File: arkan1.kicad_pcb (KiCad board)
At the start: 2 copper layers, 64.3 x 73 mm, 40 parts, among them J1 Conn_01x02, J2 USB_C_Receptacle_USB2.0_16P, J3 Conn_Coaxial, J4 Conn_Coaxial, Q1 NMOS (DSG), Q2 NMOS (CHG), Q3 PMOS, SW1 SW_Push, U1 DW01A, U2 SX1278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

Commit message: updated pcb
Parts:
- removed J3: Conn_Coaxial, Connector_Coaxial:SMA_Molex_73251-1153_EdgeMount_Horizontal
- C7: value 4.7 uF -> 1 uF
- C8: value 4.7 uF -> 1 uf
- D1, D2, D3: footprint LED_SMD:LED_0201_0603Metric -> LED_SMD:LED_0805_2012Metric
- R1, R10, R11, R13, R2, R3, R4, R5, R6, R7, R9: footprint Resistor_SMD:R_0201_0603Metric -> Resistor_SMD:R_0805_2012Metric_Pad1.20x1.40mm_HandSolder
- SW1: footprint Button_Switch_SMD:Nidec_Copal_CAS-120A -> Button_Switch_SMD:SW_SPST_PTS645Sx43SMTR92
- U2: value SX1278 -> Ai-Thinker-Ra-02; footprint Package_DFN_QFN:QFN-28-1EP_6x6mm_P0.65mm_EP4.8x4.8mm -> RF_Module:Ai-Thinker-Ra-01-LoRa
- U3: footprint Package_SO:SOIC-8-1EP_3.9x4.9mm_P1.27mm_EP2.41x3.3mm_ThermalVias -> Package_SO:SOIC-8-1EP_3.9x4.9mm_P1.27mm_EP2.41x3.81mm
- moved R4 6.60 mm to (211.6, 83.5)
- moved U2 6.08 mm to (183.7, 123.0), turned to 0 degrees
- moved C1 5.15 mm to (186.6, 87.7)
- moved L1 3.93 mm to (189.1, 110.0)
- moved R11 3.93 mm to (193.5, 110.0)
- moved C10 3.81 mm to (195.3, 92.2)
- moved R1 2.76 mm to (178.1, 81.6)
- moved SW1 2.76 mm to (179.5, 88.8)
- moved D3 1.67 mm to (189.7, 106.0)
- moved R3 1.12 mm to (192.2, 65.4)
- moved R7 1.12 mm to (192.2, 63.2)
- moved R2 1.07 mm to (198.4, 75.4)
- moved R6 1.01 mm to (211.8, 78.4)
- moved R5 0.87 mm to (211.8, 75.7)
- moved R13 0.83 mm to (178.6, 77.7)
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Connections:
- A1 pad 13: Net-(A1-GND-Pad13) -> GND
- A1 pad 18: Net-(A1-GND-Pad13) -> GND
- A1 pad 23: Net-(A1-GND-Pad13) -> GND
- A1 pad 24: Net-(A1-GPIO18) -> unconnected-(A1-GPIO18-Pad24)
- A1 pad 27: unconnected-(A1-GPIO21-Pad27) -> Net-(A1-GPIO21)
- A1 pad 3: Net-(A1-GND-Pad13) -> GND
- A1 pad 33: unconnected-(A1-AGND-Pad33) -> GND
- A1 pad 38: Net-(A1-GND-Pad13) -> GND
- A1 pad 8: Net-(A1-GND-Pad13) -> GND
- J2 pad B6: unconnected-(J2-D+-PadA6) -> unconnected-(J2-D+-PadB6)
- J2 pad B7: unconnected-(J2-D--PadA7) -> unconnected-(J2-D--PadB7)
- U2 pad 1: Net-(J3-In) -> GND
- U2 pad 12: unconnected-(U2-DIO4-Pad12) -> Net-(A1-GPIO19)
- U2 pad 13: unconnected-(U2-DIO5-Pad13) -> Net-(A1-GPIO22)
- U2 pad 14: Net-(A1-3V3) -> Net-(A1-GPIO20)
- U2 pad 15: GND -> Net-(A1-GPIO21)
- U2 pad 16: Net-(A1-GPIO19) -> GND
- U2 pad 2: unconnected-(U2-VR_ANA-Pad2) -> GND
- U2 pad 3: unconnected-(U2-VBAT_ANA-Pad3) -> Net-(A1-3V3)
- U2 pad 4: unconnected-(U2-VR_DIG-Pad4) -> Net-(A1-GPIO16)
- U2 pad 5: unconnected-(U2-XTA-Pad5) -> Net-(A1-GPIO17)
- U2 pad 7: Net-(A1-GPIO16) -> unconnected-(U2-DIO2-Pad7)
- U2 pad 8: Net-(A1-GPIO17) -> unconnected-(U2-DIO3-Pad8)
- U2 pad 9: unconnected-(U2-DIO1-Pad9) -> GND
- U3 pad 9: unconnected-(U3-EPAD-Pad9) -> GND
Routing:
- net GND: track 61.0 -> 101.2 mm, vias 0 -> 2
- net Net-(A1-3V3): track 41.1 -> 70.3 mm, vias 0 -> 2
- net Net-(A1-GPIO21): track 0.00 -> 24.6 mm
- net Net-(A1-GPIO19): track 10.9 -> 25.0 mm
- net Net-(A1-GPIO20): track 10.4 -> 24.4 mm, vias 2 -> 0
- net Net-(A1-RUN): track 34.3 -> 47.8 mm
- net Net-(A1-GPIO22): track 17.1 -> 29.7 mm
- net Net-(J3-In): track 12.5 -> 0.00 mm, vias 2 -> 0
- net Net-(A1-GPIO18): track 7.52 -> 0.00 mm
- net Net-(U3-PROG): track 28.8 -> 21.5 mm, vias 0 -> 2
- net Net-(A1-GPIO16): track 10.3 -> 4.82 mm
- net Net-(U3-CE): track 46.3 -> 40.9 mm
- net Net-(U4-RSVD_8): track 6.04 -> 8.95 mm
- net Net-(A1-GPIO17): track 13.0 -> 10.4 mm, vias 2 -> 0
- net Net-(J4-In): track 35.0 -> 37.5 mm
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
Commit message: Fix Design Rules Check on PCB + SCH
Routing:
- net Net-(U3-CE): track 40.9 -> 46.5 mm
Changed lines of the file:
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@@
+	)
+	(segment
+		(start 212.755 74.859999)
+		(end 209.37 71.474999)
+		(width 0.2)
+		(layer "F.Cu")
+		(net 48)
 	)
 	(segment
@@
 		(width 0.2)
 		(layer "F.Cu")
+		(net 48)
+	)
+	(segment
+		(start 212.755 75.65)
+		(end 212.755 74.859999)
+		(width 0.2)
+		(layer "F.Cu")

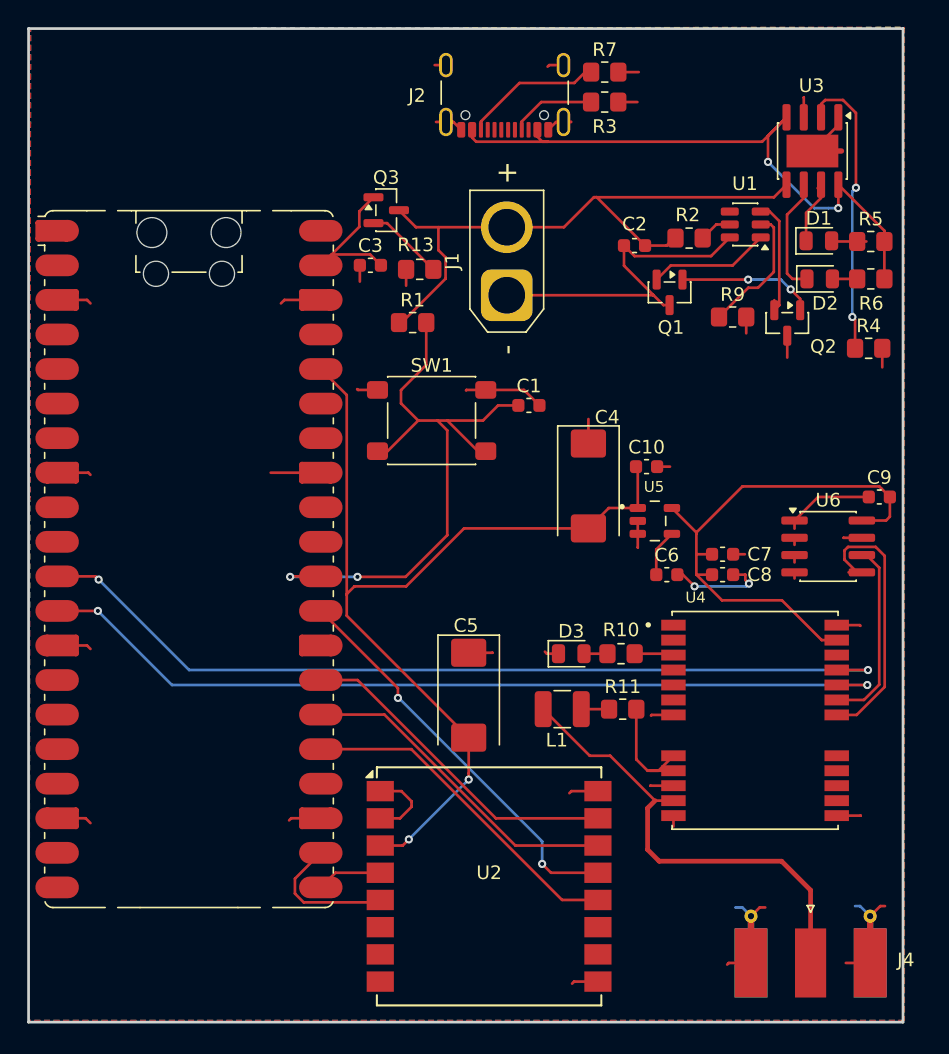
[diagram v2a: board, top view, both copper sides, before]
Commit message: Added via stitches, via fence on pcb, isolated copper fix
Also moved some components, added a small graphic on the pcb
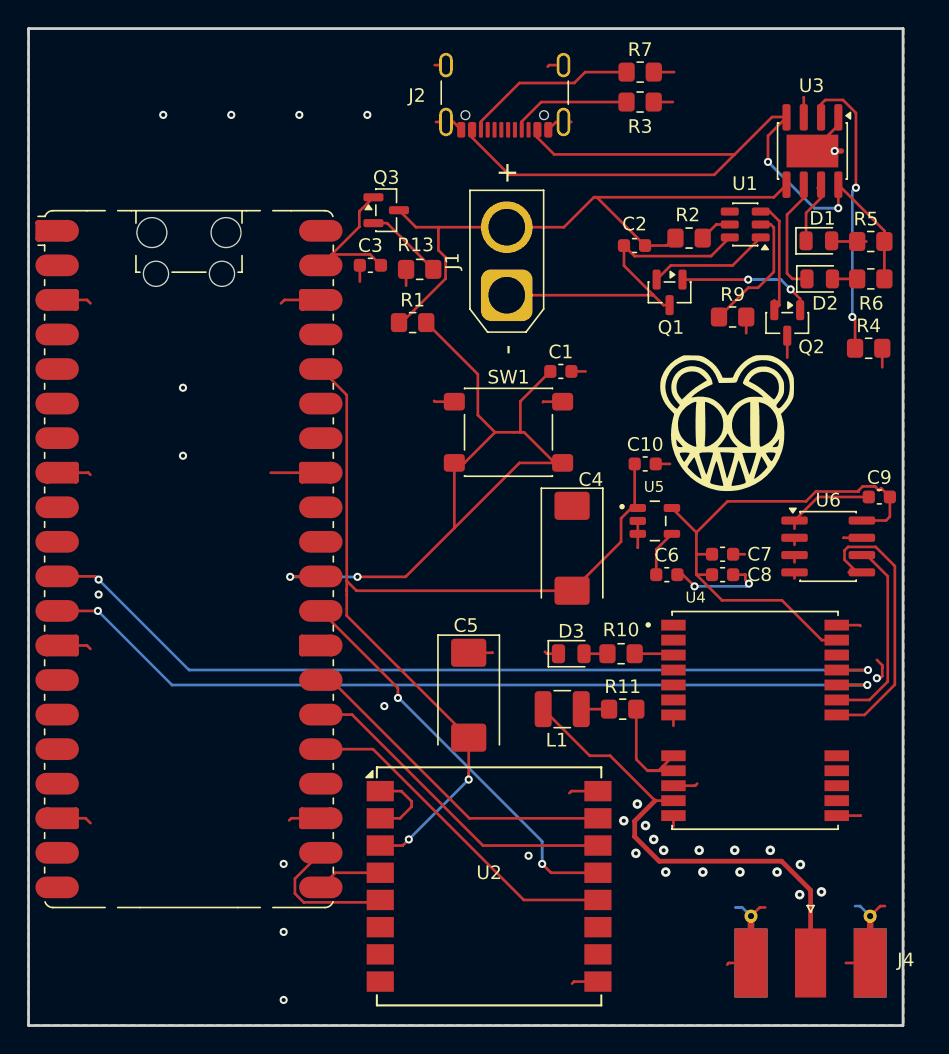
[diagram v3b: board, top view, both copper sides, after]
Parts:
- added G***: LOGO, rdhead_logo:logosmall, F.Cu at (201.2, 89.0)
- moved SW1 5.72 mm to (185.1, 89.7)
- moved C4 4.73 mm to (189.8, 98.2)
- moved C1 3.43 mm to (189.0, 85.2)
- moved R3 2.61 mm to (194.8, 65.4)
- moved R7 2.61 mm to (194.8, 63.2)
- moved C10 0.22 mm to (195.2, 92.0)
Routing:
- net Net-(U3-CE): track 46.5 -> 63.2 mm
- net Net-(A1-RUN): track 47.8 -> 55.9 mm
- net GND: track 101.2 -> 97.2 mm, vias 2 -> 32
- net Net-(J2-CC2): track 9.77 -> 12.8 mm
- net Net-(J2-CC1): track 5.86 -> 8.90 mm
- net Net-(A1-3V3): track 70.3 -> 71.7 mm
- net Net-(U4-SDA2): track 20.7 -> 21.6 mm
- net Net-(J4-In): track 37.5 -> 38.3 mm
- net Net-(U4-SCL2): track 13.9 -> 14.7 mm
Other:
- board size 64.3 x 73 mm -> 64.3 x 73.3 mm

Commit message: final pcb variant
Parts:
- added REF**: MountingHole_2.2mm_M2_DIN965_Pad, MountingHole:MountingHole_2.2mm_M2_DIN965_Pad, F.Cu at (152.6, 130.2)
- added REF**: MountingHole_2.2mm_M2_DIN965_Pad, MountingHole:MountingHole_2.2mm_M2_DIN965_Pad, F.Cu at (152.6, 62.8)
- added REF**: MountingHole_2.2mm_M2_DIN965_Pad, MountingHole:MountingHole_2.2mm_M2_DIN965_Pad, F.Cu at (211.4, 62.8)
